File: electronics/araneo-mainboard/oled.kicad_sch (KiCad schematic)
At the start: 2 parts, among them J12 OLED

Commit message: electronics: update bom
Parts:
- J12: now left out of the parts list
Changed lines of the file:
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@@
 		(body_style 1)
 		(exclude_from_sim no)
-		(in_bom yes)
+		(in_bom no)
 		(on_board yes)
 		(in_pos_files yes)

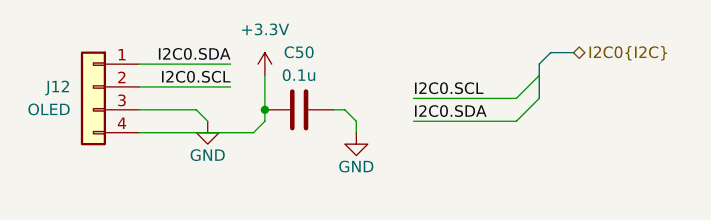
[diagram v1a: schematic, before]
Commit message: improve schematic and layout, add LCSC parts
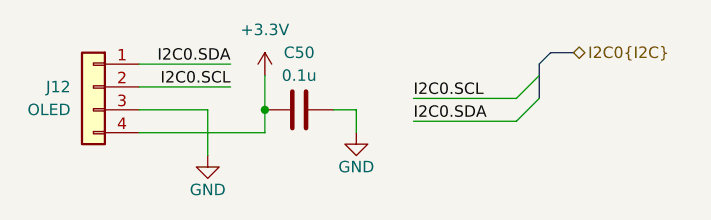
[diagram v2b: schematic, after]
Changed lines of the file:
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@@
-		)
-	)
-	(wire
-		(pts
-			(xy 160.02 73.66) (xy 158.75 74.93)
-		)
-		(stroke
-			(width 0)
-			(type default)
 		)
 	)
@@
 	(wire
 		(pts
-			(xy 146.05 74.93) (xy 158.75 74.93)
-		)
-		(stroke
-			(width 0)
-			(type default)
-		)
-	)
-	(wire
-		(pts
-			(xy 153.67 73.66) (xy 152.4 72.39)
+			(xy 153.67 72.39) (xy 153.67 77.47)
+		)
+		(stroke
+			(width 0)
+			(type default)
+		)
+	)
+	(wire
+		(pts
+			(xy 146.05 74.93) (xy 160.02 74.93)
 		)
 		(stroke
@@
 	(wire
 		(pts
-			(xy 170.18 73.66) (xy 170.18 74.93)
+			(xy 170.18 72.39) (xy 170.18 74.93)
 		)
 		(stroke
@@
 	(wire
 		(pts
-			(xy 146.05 72.39) (xy 152.4 72.39)
+			(xy 146.05 72.39) (xy 153.67 72.39)
 		)
 		(stroke
@@
 	(wire
 		(pts
-			(xy 170.18 73.66) (xy 168.91 72.39)
-		)
-		(stroke
-			(width 0)
-			(type default)
-		)
-	)
-	(wire
-		(pts
 			(xy 146.05 67.31) (xy 156.21 67.31)
 		)
@@
 	(wire
 		(pts
-			(xy 160.02 72.39) (xy 160.02 73.66)
-		)
-		(stroke
-			(width 0)
-			(type default)
-		)
-	)
-	(wire
-		(pts
-			(xy 167.64 72.39) (xy 168.91 72.39)
+			(xy 160.02 72.39) (xy 160.02 74.93)
+		)
+		(stroke
+			(width 0)
+			(type default)
+		)
+	)
+	(wire
+		(pts
+			(xy 167.64 72.39) (xy 170.18 72.39)
 		)
 		(stroke
@@
 	(symbol
 		(lib_id "PCM_SparkFun-PowerSymbol:GND")
-		(at 153.67 73.66 0)
+		(at 153.67 77.47 0)
 		(unit 1)
 		(body_style 1)
@@
 		(fields_autoplaced yes)
 		(property "Reference" "#PWR0112"
-			(at 153.67 80.01 0)
+			(at 153.67 83.82 0)
 			(hide yes)
 			(show_name no)
@@
 		)
 		(property "Value" "GND"
+			(at 153.67 81.28 0)
+			(show_name no)
+			(do_not_autoplace yes)
+			(effects
+				(font
+					(size 1.27 1.27)
+				)
+			)
+		)
+		(property "Footprint" ""
 			(at 153.67 77.47 0)
-			(show_name no)
-			(do_not_autoplace yes)
-			(effects
-				(font
-					(size 1.27 1.27)
-				)
-			)
-		)
-		(property "Footprint" ""
-			(at 153.67 73.66 0)
 			(hide yes)
 			(show_name no)
@@
 		)
 		(property "Datasheet" ""
-			(at 153.67 73.66 0)
+			(at 153.67 77.47 0)
 			(hide yes)
 			(show_name no)
@@
 		)
 		(property "Description" "Power symbol creates a global label with name \"GND\" , ground"
-			(at 153.67 82.55 0)
-			(hide yes)
-			(show_name no)
+			(at 153.67 86.36 0)
+			(hide yes)
+			(show_name no)
